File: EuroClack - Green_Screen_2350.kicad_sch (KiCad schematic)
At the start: 253 parts, among them J1 C2982548, J10 CV_OUT_4, J11 C7471773, J12 DISPLAY_CONNECTOR, J13 CV_GATE_IN_4, J14 AUDIO_OUT_1, J15 AUDIO_IN_1, J16 USB_C_Receptacle_USB2.0_14P, J17 USB_HOST, J18 Eurorack 10 pin socket, J19 C7470101, J2 AUDIO_IN_2, J20 STEMMA_QT, J21 C2856837, J22 C2856837, J23 CV_GATE_IN3, J24 CV_GATE_IN_4, J25 SM03B-SRSS-TB, J26 CV_OUT_3, J27 CV_OUT_4, J28 C2881890, J29 C7470089, J3 CV_GATE_IN_1, J4 CV_GATE_IN_2, J5 CV_GATE_IN3, J6 AUDIO_OUT_2, J7 CV_OUT_1, J8 CV_OUT_2, J9 CV_OUT_3, Q1 A3400A, Q2 A3401A, Q3 A3401A, Q4 A3400A, SW3 RotaryEncoder_Switch, SW4 RotaryEncoder_Switch, SW5 USER2, SW6 SW_Push, SW7 SW_Push, U1 RP2350_80QFN, U10 SPX3819M5-L-5-0, U11 TL072, U12 TPS54302, U13 TL072, U14 SPX3819M5-L-3-3, U15 SRAM, U16 SPX3819M5-L-3-3, U17 TL072, U18 SN74LVC1T45DCK, U19 LM393, U2 PCM5102, U20 TL072, U21 LM393, U22 SN74LVC1T45DCK, U23 TPS54302, U3 MCP4728, U4 W25Q128JVS, U5 PCM1808PWR, U6 TL072, U7 REF3033, U8 TL072, U9 SPX3819M5-L-3-3, Y1 ABM8-272-T3

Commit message: work on connectors layout
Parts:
- added J30: FFC, green_screen:FPC-SMD_F1004-H-08-20G-R, symbol Connector_Generic:Conn_01x08
- J12: value DISPLAY_CONNECTOR -> Pin Header
- J16: footprint Clacktronics:918-418K2022Y40000 -> green_screen:USB-C-TH_TYPE-C-USB-14P
- J17: footprint Connector_USB:USB_A_Molex_105057_Vertical -> green_screen:USB-A-SMD_AF180-13.1
- SW3, SW4: footprint Rotary_Encoder:RotaryEncoder_Alps_EC12E-Switch_Vertical_H20mm_CircularMountingHoles -> green_screen:SW-TH_EC11XXXXXXXX
- SW5, SW6, SW7: footprint green_screen:KEY-SMD_4P-L6.0-W6.0-P3.90-LS9.0 -> green_screen:SW-TH_4P-L5.0-W5.0-P4.50-LS6.5
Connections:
- net 12V_JACK: now also J22.24 (Pin_24); no longer J22.17 (Pin_17)
- net 3V3_SD_SCREEN: now also J30.2 (Pin_2)
- net 5V_JACK: now also J22.23 (Pin_23); no longer J22.18 (Pin_18)
- net AUDIO_IN_1_JACK: now also J22.40 (Pin_40); no longer J22.1 (Pin_1)
- net AUDIO_IN_2_JACK: now also J22.39 (Pin_39); no longer J22.2 (Pin_2)
- net AUDIO_OUT_1_JACK: now also J22.38 (Pin_38); no longer J22.3 (Pin_3)
- net AUDIO_OUT_2_JACK: now also J22.37 (Pin_37); no longer J22.4 (Pin_4)
- net CV_GATE_IN_3_JACK: now also J22.36 (Pin_36); no longer J22.5 (Pin_5)
- net CV_GATE_IN_4_JACK: now also J22.35 (Pin_35); no longer J22.6 (Pin_6)
- net CV_IN_1_JACK: now also J22.26 (Pin_26); no longer J22.15 (Pin_15)
- net CV_IN_2_JACK: now also J22.25 (Pin_25); no longer J22.16 (Pin_16)
- net CV_OUT_1_JACK: now also J22.1 (Pin_1); no longer J22.40 (Pin_40)
- net CV_OUT_2_JACK: now also J22.4 (Pin_4); no longer J22.37 (Pin_37)
- net CV_OUT_3_JACK: now also J22.2 (Pin_2); no longer J22.39 (Pin_39)
- net CV_OUT_4_JACK: now also J22.3 (Pin_3); no longer J22.38 (Pin_38)
- net DISPLAY_BLK_JACK: now also J22.16 (Pin_16), J30.8 (Pin_8); no longer J22.25 (Pin_25)
- net DISPLAY_CS_JACK: now also J22.20 (Pin_20), J30.7 (Pin_7); no longer J22.21 (Pin_21)
- net DISPLAY_DC_JACK: now also J22.21 (Pin_21), J30.6 (Pin_6); no longer J22.20 (Pin_20)
- net DISPLAY_RES_JACK: now also J22.17 (Pin_17), J30.5 (Pin_5); no longer J22.24 (Pin_24)
- net DISPLAY_SCL_JACK: now also J22.19 (Pin_19), J30.3 (Pin_3); no longer J22.22 (Pin_22)
- net DISPLAY_SDA_JACK: now also J22.18 (Pin_18), J30.4 (Pin_4); no longer J22.23 (Pin_23)
- net ENC1_A_JACK: now also J22.10 (Pin_10); no longer J22.31 (Pin_31)
- net ENC1_B_JACK: now also J22.9 (Pin_9); no longer J22.32 (Pin_32)
- net ENC1_SW_JACK: now also J22.11 (Pin_11); no longer J22.30 (Pin_30)
- net ENC2_A_JACK: now also J22.7 (Pin_7); no longer J22.34 (Pin_34)
- net ENC2_B_JACK: now also J22.6 (Pin_6); no longer J22.35 (Pin_35)
- net ENC2_SW_JACK: now also J22.8 (Pin_8); no longer J22.33 (Pin_33)
- net GATE_IN_1_JACK: now also J22.34 (Pin_34); no longer J22.7 (Pin_7)
- net GATE_IN_2_JACK: now also J22.33 (Pin_33); no longer J22.8 (Pin_8)
- net GATE_OUT_1_JACK: now also J22.28 (Pin_28); no longer J22.13 (Pin_13)
- net GATE_OUT_2_JACK: now also J22.27 (Pin_27); no longer J22.14 (Pin_14)
- net GND_JACK: now also J22.22 (Pin_22), J30.1 (Pin_1); no longer J22.19 (Pin_19)
- net SW_RUN_JACK: now also J22.14 (Pin_14); no longer J22.27 (Pin_27)
- net SW_USR1_JACK: now also J22.13 (Pin_13); no longer J22.28 (Pin_28)
- net SW_USR2_JACK: now also J22.12 (Pin_12); no longer J22.29 (Pin_29)
- net USB_DM_JACK: now also J22.29 (Pin_29); no longer J22.12 (Pin_12)
- net USB_DP_JACK: now also J22.30 (Pin_30); no longer J22.11 (Pin_11)
- net USB_HOST_DM_JACK: now also J22.31 (Pin_31); no longer J22.10 (Pin_10)
- net USB_HOST_DP_JACK: now also J22.32 (Pin_32); no longer J22.9 (Pin_9)
- net ~{SW_MENU_BOOT_JACK}: now also J22.15 (Pin_15); no longer J22.26 (Pin_26)
- net ~{USBH_PWR_EN_JACK}: now also J22.5 (Pin_5); no longer J22.36 (Pin_36)
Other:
- note added: "C2758340"
- note added: "C2845268"
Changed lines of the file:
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@@
 		)
 	)
+	(text "C2845268"
+		(exclude_from_sim no)
+		(at 639.064 85.852 0)
+		(effects
+			(font
+				(size 1.27 1.27)
+			)
+		)
+	)
 	(text "JACK BOARD"
 		(exclude_from_sim no)
@@
 		)
 	)
+	(text "C2758340"
+		(exclude_from_sim no)
+		(at 547.37 138.684 0)
+		(effects
+			(font
+				(size 1.27 1.27)
+			)
+		)
+	)
 	(text "+Audio L IN"
 		(exclude_from_sim no)
@@
 	)
 	(junction
+		(at 528.32 130.81)
+		(diameter 0)
+		(color 0 0 0 0)
+	)
+	(junction
 		(at 414.02 463.55)
 		(diameter 0)
@@
 	)
 	(junction
+		(at 528.32 125.73)
+		(diameter 0)
+		(color 0 0 0 0)
+	)
+	(junction
 		(at 553.72 336.55)
 		(diameter 0)
@@
 	)
 	(junction
+		(at 528.32 120.65)
+		(diameter 0)
+		(color 0 0 0 0)
+	)
+	(junction
 		(at 614.68 209.55)
 		(diameter 0)
@@
 	)
 	(junction
+		(at 528.32 123.19)
+		(diameter 0)
+		(color 0 0 0 0)
+	)
+	(junction
 		(at 541.02 189.23)
 		(diameter 0)
@@
 	)
 	(junction
+		(at 528.32 128.27)
+		(diameter 0)
+		(color 0 0 0 0)
+	)
+	(junction
 		(at 314.96 162.56)
 		(diameter 0)
@@
 	)
 	(junction
+		(at 528.32 118.11)
+		(diameter 0)
+		(color 0 0 0 0)
+	)
+	(junction
 		(at 367.03 478.79)
 		(diameter 0)
@@
 	)
 	(junction
+		(at 528.32 135.89)
+		(diameter 0)
+		(color 0 0 0 0)
+	)
+	(junction
 		(at 520.7 462.28)
 		(diameter 0)
@@
 	)
 	(junction
+		(at 528.32 133.35)
+		(diameter 0)
+		(color 0 0 0 0)
+	)
+	(junction
 		(at 289.56 242.57)
 		(diameter 0)
@@
 	(wire
 		(pts
+			(xy 528.32 120.65) (xy 541.02 120.65)
+		)
+		(stroke
+			(width 0)
+			(type default)
+		)
+	)
+	(wire
+		(pts
 			(xy 687.07 316.23) (xy 690.88 316.23)
 		)
@@
 	(wire
 		(pts
+			(xy 528.32 125.73) (xy 541.02 125.73)
+		)
+		(stroke
+			(width 0)
+			(type default)
+		)
+	)
+	(wire
+		(pts
 			(xy 678.18 260.35) (xy 670.56 260.35)
 		)
@@
 	(wire
 		(pts
+			(xy 528.32 118.11) (xy 541.02 118.11)
+		)
+		(stroke
+			(width 0)
+			(type default)
+		)
+	)
+	(wire
+		(pts
 			(xy 397.51 138.43) (xy 407.67 138.43)
 		)
@@
 	(wire
 		(pts
+			(xy 528.32 135.89) (xy 541.02 135.89)
+		)
+		(stroke
+			(width 0)
+			(type default)
+		)
+	)
+	(wire
+		(pts
 			(xy 199.39 377.19) (xy 219.71 377.19)
 		)
@@
 	(wire
 		(pts
+			(xy 528.32 130.81) (xy 541.02 130.81)
+		)
+		(stroke
+			(width 0)
+			(type default)
+		)
+	)
+	(wire
+		(pts
 			(xy 589.28 300.99) (xy 589.28 306.07)
 		)
@@
 	(wire
 		(pts
+			(xy 528.32 133.35) (xy 541.02 133.35)
+		)
+		(stroke
+			(width 0)
+			(type default)
+		)
+	)
+	(wire
+		(pts
 			(xy 563.88 265.43) (xy 567.69 265.43)
 		)
@@
 	(wire
 		(pts
+			(xy 528.32 128.27) (xy 541.02 128.27)
+		)
+		(stroke
+			(width 0)
+			(type default)
+		)
+	)
+	(wire
+		(pts
 			(xy 105.41 431.8) (xy 109.22 431.8)
 		)
@@
 	(wire
 		(pts
+			(xy 528.32 123.19) (xy 541.02 123.19)
+		)
+		(stroke
+			(width 0)
+			(type default)
+		)
+	)
+	(wire
+		(pts
 			(xy 680.72 533.4) (xy 702.31 533.4)
 		)
@@
 			)
 		)
-		(property "Value" "DISPLAY_CONNECTOR"
+		(property "Value" "Pin Header"
 			(at 510.794 111.506 0)
 			(effects
@@
 			)
 		)
-		(property "Footprint" "Rotary_Encoder:RotaryEncoder_Alps_EC12E-Switch_Vertical_H20mm_CircularMountingHoles"
+		(property "Footprint" "green_screen:SW-TH_EC11XXXXXXXX"
 			(at 563.88 70.866 0)
 			(effects
@@
 			)
 		)
-		(property "Footprint" "green_screen:KEY-SMD_4P-L6.0-W6.0-P3.90-LS9.0"
+		(property "Footprint" "green_screen:SW-TH_4P-L5.0-W5.0-P4.50-LS6.5"
 			(at 706.12 66.04 0)
 			(effects
@@
 	(symbol
 		(lib_id "Connector_Generic:Conn_01x40")
-		(at 675.64 518.16 0)
-		(mirror y)
+		(at 675.64 520.7 180)
 		(unit 1)
 		(exclude_from_sim no)
@@
 		(dnp no)
 		(property "Reference" "J22"
-			(at 673.608 518.2178 0)
+			(at 673.608 520.6422 0)
 			(effects
 				(font
@@
 		)
 		(property "Value" "C2856837"
-			(at 673.608 520.6421 0)
+			(at 673.608 518.2179 0)
 			(effects
 				(font
@@
 		)
 		(property "Footprint" "green_screen:FPC-SMD_40P-P0.50_XUNPU_FPC-05FB-40PH20"
-			(at 675.64 518.16 0)
+			(at 675.64 520.7 0)
 			(effects
 				(font
@@
 		)
 		(property "Datasheet" "~"
-			(at 675.64 518.16 0)
+			(at 675.64 520.7 0)
 			(effects
 				(font
@@
 		)
 		(property "Description" "Generic connector, single row, 01x40, script generated (kicad-library-utils/schlib/autogen/connector/)"
-			(at 675.64 518.16 0)
+			(at 675.64 520.7 0)
 			(effects
 				(font
@@
 			)
 		)
-		(property "Footprint" "Connector_USB:USB_A_Molex_105057_Vertical"
+		(property "Footprint" "green_screen:USB-A-SMD_AF180-13.1"
 			(at 635 132.08 0)
 			(effects
@@
 			)
 		)
-		(property "Footprint" "green_screen:KEY-SMD_4P-L6.0-W6.0-P3.90-LS9.0"
+		(property "Footprint" "green_screen:SW-TH_4P-L5.0-W5.0-P4.50-LS6.5"
 			(at 622.3 79.375 0)
 			(effects
@@
 			)
 		)
-		(property "Footprint" "green_screen:KEY-SMD_4P-L6.0-W6.0-P3.90-LS9.0"
+		(property "Footprint" "green_screen:SW-TH_4P-L5.0-W5.0-P4.50-LS6.5"
 			(at 607.06 43.18 0)
 			(effects
@@
 			)
 		)
-		(property "Footprint" "Rotary_Encoder:RotaryEncoder_Alps_EC12E-Switch_Vertical_H20mm_CircularMountingHoles"
+		(property "Footprint" "green_screen:SW-TH_EC11XXXXXXXX"
 			(at 563.88 53.086 0)
 			(effects
@@
 			)
 		)
-		(property "Footprint" "Clacktronics:918-418K2022Y40000"
+		(property "Footprint" "green_screen:USB-C-TH_TYPE-C-USB-14P"
 			(at 166.37 187.96 0)
 			(effects
@@
 					(unit 1)
 				)
+			)
+		)
+	)
+	(symbol
+		(lib_id "Connector_Generic:Conn_01x08")
+		(at 546.1 125.73 0)
+		(unit 1)
+		(exclude_from_sim no)
+		(in_bom yes)
+		(on_board yes)
+		(dnp no)
+		(property "Reference" "J30"
+			(at 548.132 125.7878 0)
+			(effects
+				(font
+					(size 1.27 1.27)
+				)
+				(justify left)
+			)
+		)
+		(property "Value" "FFC"
+			(at 544.322 113.03 0)
+			(effects
+				(font
+					(size 1.27 1.27)
+				)
+				(justify left)
+			)
+		)
+		(property "Footprint" "green_screen:FPC-SMD_F1004-H-08-20G-R"
+			(at 546.1 125.73 0)
+			(effects
+				(font
+					(size 1.27 1.27)
+				)
+				(hide yes)
+			)
+		)
+		(property "Datasheet" "~"
+			(at 546.1 125.73 0)
+			(effects
+				(font
+					(size 1.27 1.27)
+				)
+				(hide yes)
+			)
+		)
+		(property "Description" "Generic connector, single row, 01x08, script generated (kicad-library-utils/schlib/autogen/connector/)"
+			(at 546.1 125.73 0)
+			(effects
+				(font
+					(size 1.27 1.27)
+				)
+				(hide yes)
+			)
+		)
+		(pin "1"
+		)
+		(pin "4"
+		)
+		(pin "3"
+		)
+		(pin "5"
+		)
+		(pin "6"
+		)
+		(pin "7"
+		)
+		(pin "2"
+		)
+		(pin "8"
+		)
+		(instances
+			(project "EuroClack - Green_Screen_2350"
+				(path "/6f5038df-e76f-49bd-844a-6b4074e990d8"
+					(reference "J30")
+					(unit 1)
+				)

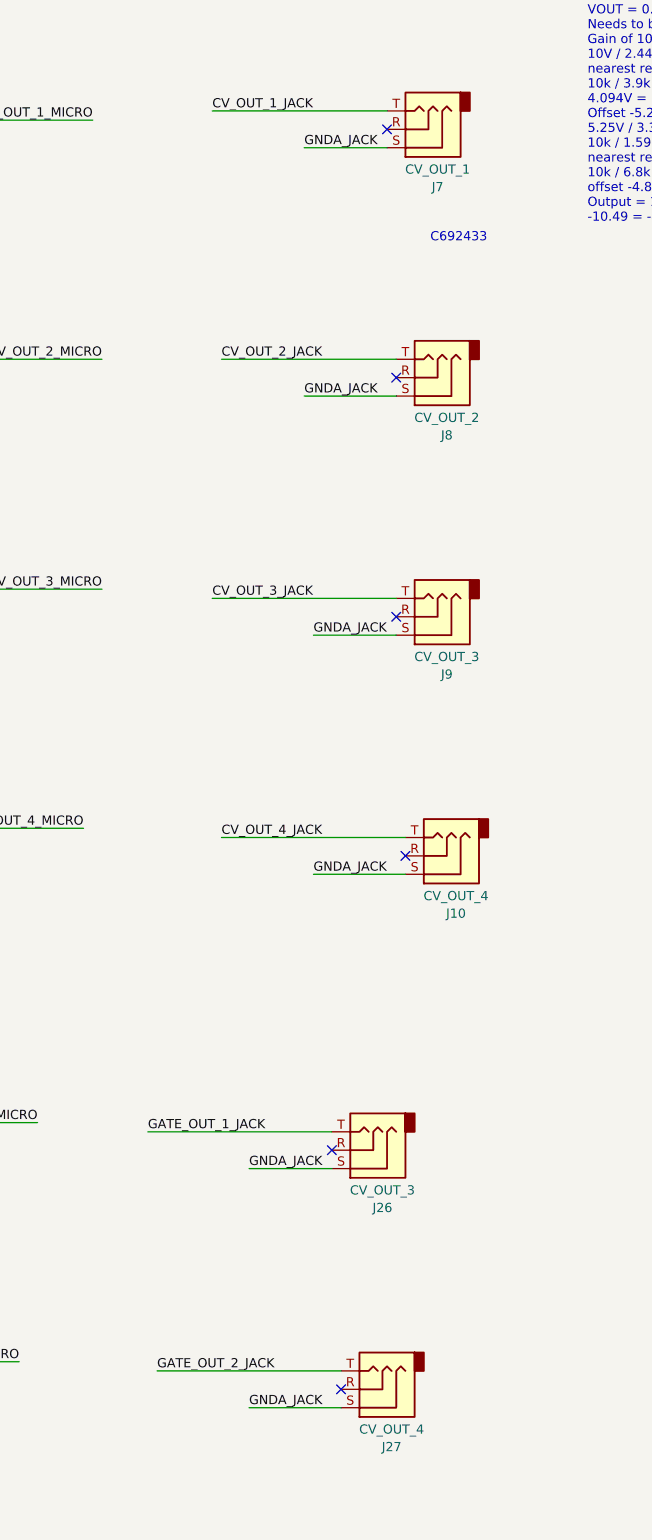
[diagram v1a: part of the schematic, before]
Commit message: Added ground pour to panel and asjusted nets to suit
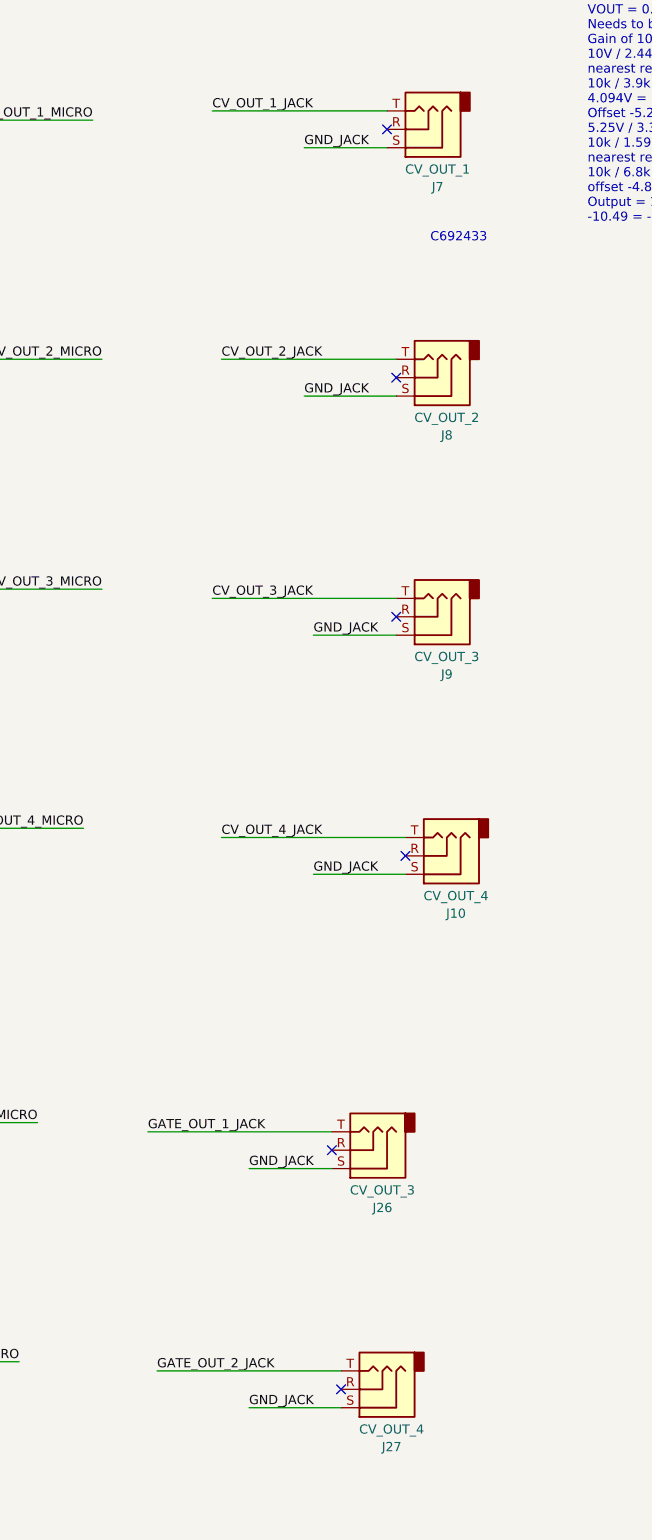
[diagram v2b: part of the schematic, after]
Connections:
- net GNDA_JACK: no longer J10.S, J26.S, J27.S, J7.S, J8.S, J9.S
- net GND_JACK: now also J10.S, J26.S, J27.S, J7.S, J8.S, J9.S
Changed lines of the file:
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@@
-		)
-	)
-	(label "GNDA_JACK"
-		(at 777.24 309.88 0)
-		(effects
-			(font
-				(size 1.27 1.27)
-			)
-			(justify left bottom)
 		)
 	)
@@
 		)
 	)
+	(label "GND_JACK"
+		(at 778.51 342.9 0)
+		(effects
+			(font
+				(size 1.27 1.27)
+			)
+			(justify left bottom)
+		)
+	)
 	(label "VREF_ADC_NEG"
 		(at 647.7 304.8 0)
@@
 		)
 	)
-	(label "GNDA_JACK"
-		(at 778.51 375.92 0)
-		(effects
-			(font
-				(size 1.27 1.27)
-			)
-			(justify left bottom)
-		)
-	)
 	(label "MCU_GATE_OUT_2"
 		(at 628.65 443.23 0)
@@
 		)
 	)
+	(label "GND_JACK"
+		(at 769.62 416.56 0)
+		(effects
+			(font
+				(size 1.27 1.27)
+			)
+			(justify left bottom)
+		)
+	)
 	(label "USB_DP_JACK"
 		(at 198.12 190.5 180)
@@
 		)
 	)
-	(label "GNDA_JACK"
-		(at 778.51 342.9 0)
-		(effects
-			(font
-				(size 1.27 1.27)
-			)
-			(justify left bottom)
-		)
-	)
 	(label "MCU_GATE_OUT_1"
 		(at 519.43 274.32 180)
@@
 		)
 	)
+	(label "GND_JACK"
+		(at 777.24 309.88 0)
+		(effects
+			(font
+				(size 1.27 1.27)
+			)
+			(justify left bottom)
+		)
+	)
 	(label "HSTX16_RST"
 		(at 645.16 528.32 0)
@@
 		)
 	)
-	(label "GNDA_JACK"
+	(label "GND_JACK"
 		(at 769.62 449.58 0)
 		(effects
@@
 		)
 	)
-	(label "GNDA_JACK"
-		(at 777.24 275.59 0)
-		(effects
-			(font
-				(size 1.27 1.27)
-			)
-			(justify left bottom)
-		)
-	)
 	(label "SWD"
 		(at 381 318.77 0)
@@
 		)
 	)
-	(label "GNDA_JACK"
-		(at 769.62 416.56 0)
-		(effects
-			(font
-				(size 1.27 1.27)
-			)
-			(justify left bottom)
-		)
-	)
 	(label "DISPLAY_DC_JACK"
 		(at 701.04 518.16 180)
@@
 		)
 	)
+	(label "GND_JACK"
+		(at 777.24 275.59 0)
+		(effects
+			(font
+				(size 1.27 1.27)
+			)
+			(justify left bottom)
+		)
+	)
 	(label "XOUT"
 		(at 419.1 269.24 0)
@@
 		)
 	)
+	(label "GND_JACK"
+		(at 778.51 375.92 0)
+		(effects
+			(font
+				(size 1.27 1.27)
+			)
+			(justify left bottom)
+		)
+	)

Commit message: little bits
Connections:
- net GND: no longer SW6.1, SW7.1
- net GND_JACK: now also SW6.1, SW7.1
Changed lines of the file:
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@@
 	(wire
 		(pts
+			(xy 627.38 84.455) (xy 627.38 92.71)
+		)
+		(stroke
+			(width 0)
+			(type default)
+		)
+	)
+	(wire
+		(pts
 			(xy 657.86 165.1) (xy 675.64 165.1)
 		)
@@
 	(wire
 		(pts
-			(xy 627.38 84.455) (xy 627.38 86.36)
-		)
-		(stroke
-			(width 0)
-			(type default)
-		)
-	)
-	(wire
-		(pts
 			(xy 222.25 511.81) (xy 233.68 511.81)
 		)
@@
 	(wire
 		(pts
-			(xy 612.14 48.26) (xy 612.14 52.07)
-		)
-		(stroke
-			(width 0)
-			(type default)
-		)
-	)
-	(wire
-		(pts
 			(xy 476.25 198.12) (xy 478.79 198.12)
 		)
@@
 	(wire
 		(pts
+			(xy 612.14 48.26) (xy 612.14 57.15)
+		)
+		(stroke
+			(width 0)
+			(type default)
+		)
+	)
+	(wire
+		(pts
 			(xy 503.555 389.255) (xy 503.555 387.35)
 		)
@@
 		)
 	)
+	(label "GND_JACK"
+		(at 612.14 57.15 90)
+		(effects
+			(font
+				(size 1.27 1.27)
+			)
+			(justify left bottom)
+		)
+	)
 	(label "GATE_IN_2_MICRO"
 		(at 643.89 487.68 0)
@@
 		)
 	)
+	(label "GND_JACK"
+		(at 627.38 92.71 90)
+		(effects
+			(font
+				(size 1.27 1.27)
+			)
+			(justify left bottom)
+		)
+	)
 	(label "CV_OUT_2_MICRO"
 		(at 749.3 304.8 180)
@@
 	)
 	(symbol
-		(lib_id "power:GND")
-		(at 612.14 52.07 0)
-		(unit 1)
-		(exclude_from_sim no)
-		(in_bom yes)
-		(on_board yes)
-		(dnp no)
-		(property "Reference" "#PWR0127"
-			(at 612.14 58.42 0)
-			(effects
-				(font
-					(size 1.27 1.27)
-				)
-				(hide yes)
-			)
-		)
-		(property "Value" "GND"
-			(at 612.267 56.4642 0)
-			(effects
-				(font
-					(size 1.27 1.27)
-				)
-			)
-		)
-		(property "Footprint" ""
-			(at 612.14 52.07 0)
-			(effects
-				(font
-					(size 1.27 1.27)
-				)
-				(hide yes)
-			)
-		)
-		(property "Datasheet" ""
-			(at 612.14 52.07 0)
-			(effects
-				(font
-					(size 1.27 1.27)
-				)
-				(hide yes)
-			)
-		)
-		(property "Description" ""
-			(at 612.14 52.07 0)
-			(effects
-				(font
-					(size 1.27 1.27)
-				)
-			)
-		)
-		(pin "1"
-		)
-		(instances
-			(project "EuroClack - Green_Screen_2350"
-				(path "/6f5038df-e76f-49bd-844a-6b4074e990d8"
-					(reference "#PWR0127")
-					(unit 1)
-				)
-			)
-		)
-	)
-	(symbol
 		(lib_id "Device:FerriteBead_Small")
 		(at 689.61 210.82 90)
@@
 					(unit 1)
 				)
-			)
-		)
-	)
-	(symbol
-		(lib_id "power:GND")
-		(at 627.38 86.36 0)
-		(unit 1)
-		(exclude_from_sim no)
-		(in_bom yes)
-		(on_board yes)
-		(dnp no)
-		(property "Reference" "#PWR0159"
-			(at 627.38 92.71 0)
-			(effects
-				(font
-					(size 1.27 1.27)
-				)
-				(hide yes)
-			)
-		)
-		(property "Value" "GND"
-			(at 627.507 90.7542 0)
-			(effects
-				(font
-					(size 1.27 1.27)
-				)
-			)
-		)
-		(property "Footprint" ""
-			(at 627.38 86.36 0)
-			(effects
-				(font
-					(size 1.27 1.27)
-				)
-				(hide yes)
-			)
-		)
-		(property "Datasheet" ""
-			(at 627.38 86.36 0)
-			(effects
-				(font
-					(size 1.27 1.27)
-				)
-				(hide yes)
-			)
-		)
-		(property "Description" ""
-			(at 627.38 86.36 0)
-			(effects
-				(font
-					(size 1.27 1.27)
-				)
-			)
-		)
-		(pin "1"
-		)
-		(instances
-			(project "EuroClack - Green_Screen_2350"
-				(path "/6f5038df-e76f-49bd-844a-6b4074e990d8"
-					(reference "#PWR0159")
-					(unit 1)
-				)

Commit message: Tweaks
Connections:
- net GND: no longer C85.1, C87.2, C88.2, C89.2, R98.1, U23.1 (GND)
- net GND_JACK: now also C85.1, C87.2, C88.2, C89.2, R98.1, U23.1 (GND)
